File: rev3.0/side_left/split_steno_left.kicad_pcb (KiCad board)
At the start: 2 copper layers, 99.7 x 72.2 mm, 31 parts, among them J1 USB_B, J2 Audio-Jack-4, P1 TC2030-IDC, SW1 SW_Push, SW10 SW_Push, SW11 SW_Push, SW12 SW_Push, SW13 SW_Push, SW14 SW_Push, SW15 SW_Push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

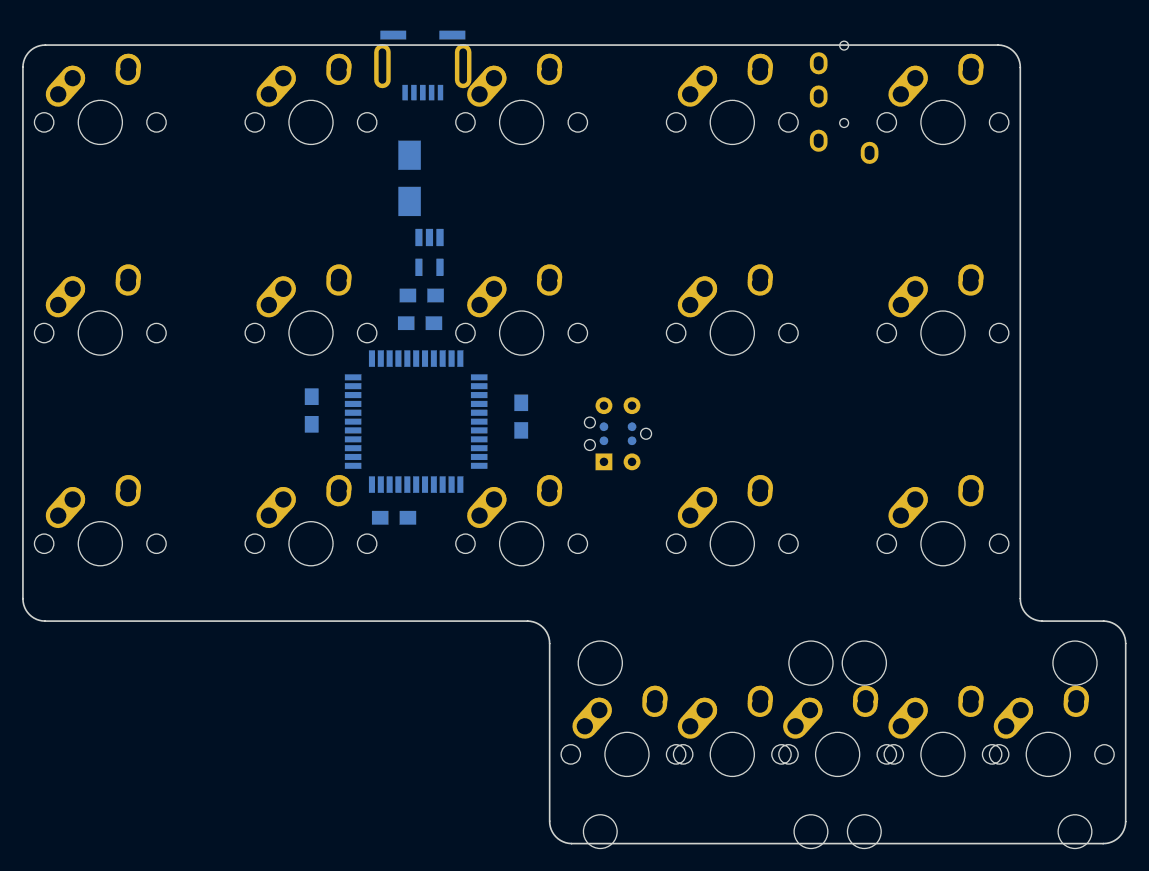
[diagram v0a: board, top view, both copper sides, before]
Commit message: added edge cuts, and mounting holes
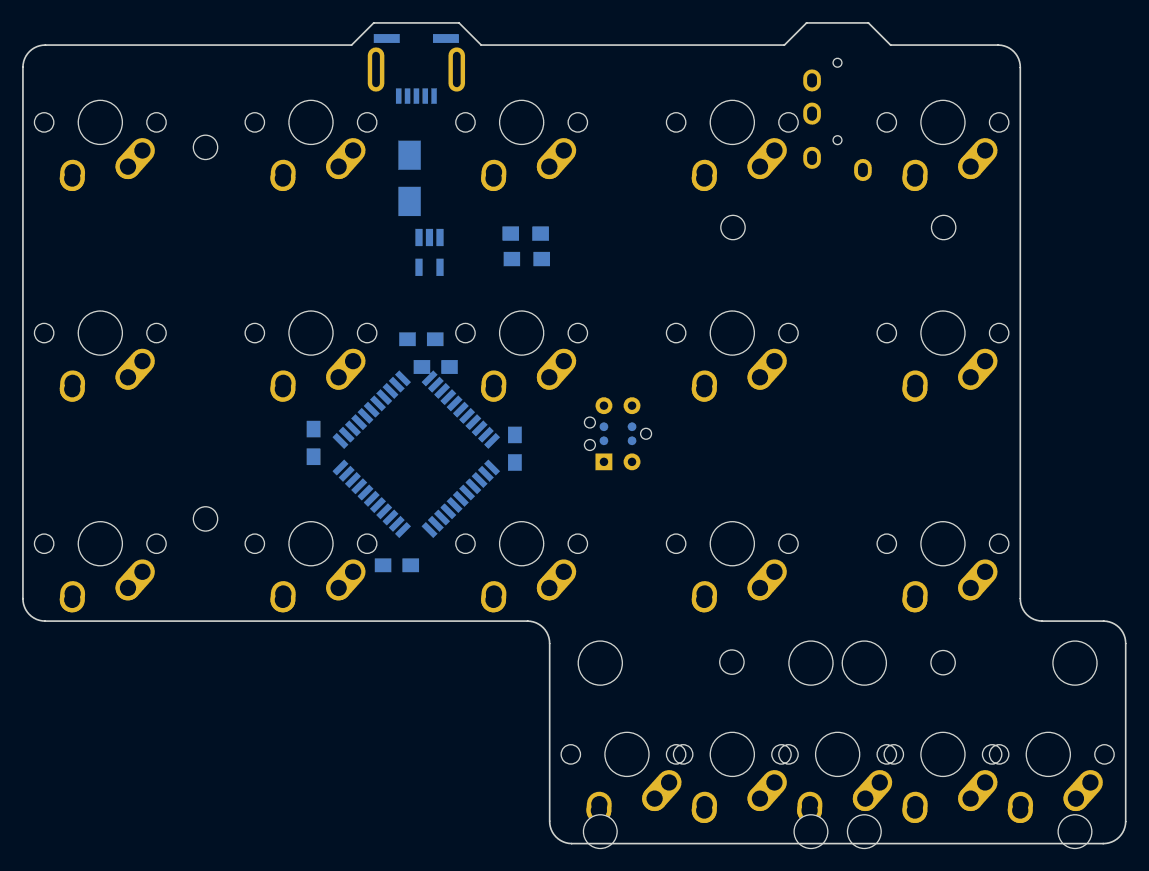
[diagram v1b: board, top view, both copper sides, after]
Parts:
- added G***: LOGO, lib_fp:lotus, B.Cu at (97.9, 56.2)
- added M2: MountingHole_2.2mm_M2, Mounting_Holes:MountingHole_2.2mm_M2, F.Cu at (128.6, 94.1)
- added M2: MountingHole_2.2mm_M2, Mounting_Holes:MountingHole_2.2mm_M2, F.Cu at (109.5, 94.0)
- added M2: MountingHole_2.2mm_M2, Mounting_Holes:MountingHole_2.2mm_M2, F.Cu at (128.7, 54.8)
- added M2: MountingHole_2.2mm_M2, Mounting_Holes:MountingHole_2.2mm_M2, F.Cu at (109.6, 54.8)
- added M2: MountingHole_2.2mm_M2, Mounting_Holes:MountingHole_2.2mm_M2, F.Cu at (61.9, 81.1)
- added M2: MountingHole_2.2mm_M2, Mounting_Holes:MountingHole_2.2mm_M2, F.Cu at (61.9, 47.5)
- added R1: 4.7k, Resistors_SMD:R_0805_HandSoldering, B.Cu at (91.0, 57.6)
- added R2: 4.7k, Resistors_SMD:R_0805_HandSoldering, B.Cu at (90.8, 55.3)
- SW19, SW20: footprint MX_Alps_Hybrid:MX-2U-ReversedStabilizers-NoLED -> MX_Alps_Hybrid:MX-2U-NoLED
- moved C2 4.31 mm to (79.2, 85.3)
- moved C1 4.21 mm to (82.7, 67.4)
- moved C4 3.95 mm to (81.4, 64.8)
- moved C5 2.96 mm to (89.9, 74.8)
- moved U2 2.95 mm to (81.0, 75.2), turned to 45 degrees
- moved C3 2.93 mm to (71.7, 74.2)
- moved J2 1.66 mm to (119.0, 38.2)
- moved J1 0.66 mm to (81.0, 42.9)
- turned SW1 to 180 degrees
- turned SW10 to 180 degrees
- turned SW11 to 180 degrees
- turned SW12 to 180 degrees
- turned SW13 to 180 degrees
- turned SW14 to 180 degrees
- turned SW15 to 180 degrees
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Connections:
- J2 pad 1: Net-(J2-Pad1) -> VCC
- J2 pad 2: Net-(J2-Pad2) -> /SCL
- J2 pad 3: Net-(J2-Pad3) -> /SDA
- U2 pad 28: Net-(U2-Pad28) -> /SDA
- U2 pad 29: Net-(U2-Pad29) -> /SCL
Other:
- board size 99.7 x 72.2 mm -> 99.7 x 74.2 mm

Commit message: things (i forgot what changed)
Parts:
- removed G***: LOGO, lib_fp:lotus
- C1, C2, C3, C4, C5: footprint Capacitors_SMD:C_0805_HandSoldering -> Capacitors_SMD:C_0603_HandSoldering
- R1, R2: footprint Resistors_SMD:R_0805_HandSoldering -> Resistors_SMD:R_0603_HandSoldering
- moved C2 12.7 mm to (73.2, 74.1), turned to 270 degrees
- moved C4 12.4 mm to (88.7, 74.9), turned to 90 degrees
- moved C3 11.3 mm to (79.0, 82.9), turned to 0 degrees
- moved C5 10.9 mm to (83.0, 66.3), turned to 180 degrees
- moved F1 8.63 mm to (76.3, 58.0), turned to 0 degrees
- moved U1 6.29 mm to (77.7, 61.4), turned to 0 degrees
- moved C1 0.41 mm to (83.0, 67.7)
- moved U2 0.05 mm to (81.0, 75.3), turned to 90 degrees
